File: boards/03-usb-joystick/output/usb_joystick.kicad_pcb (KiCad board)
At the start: 2 copper layers, 80 x 60 mm, 19 parts, among them J1 USB-C, J2 Joystick, SW1 Button, SW2 Button, SW3 Button, SW4 Button, U1 MCU, Y1 16MHz

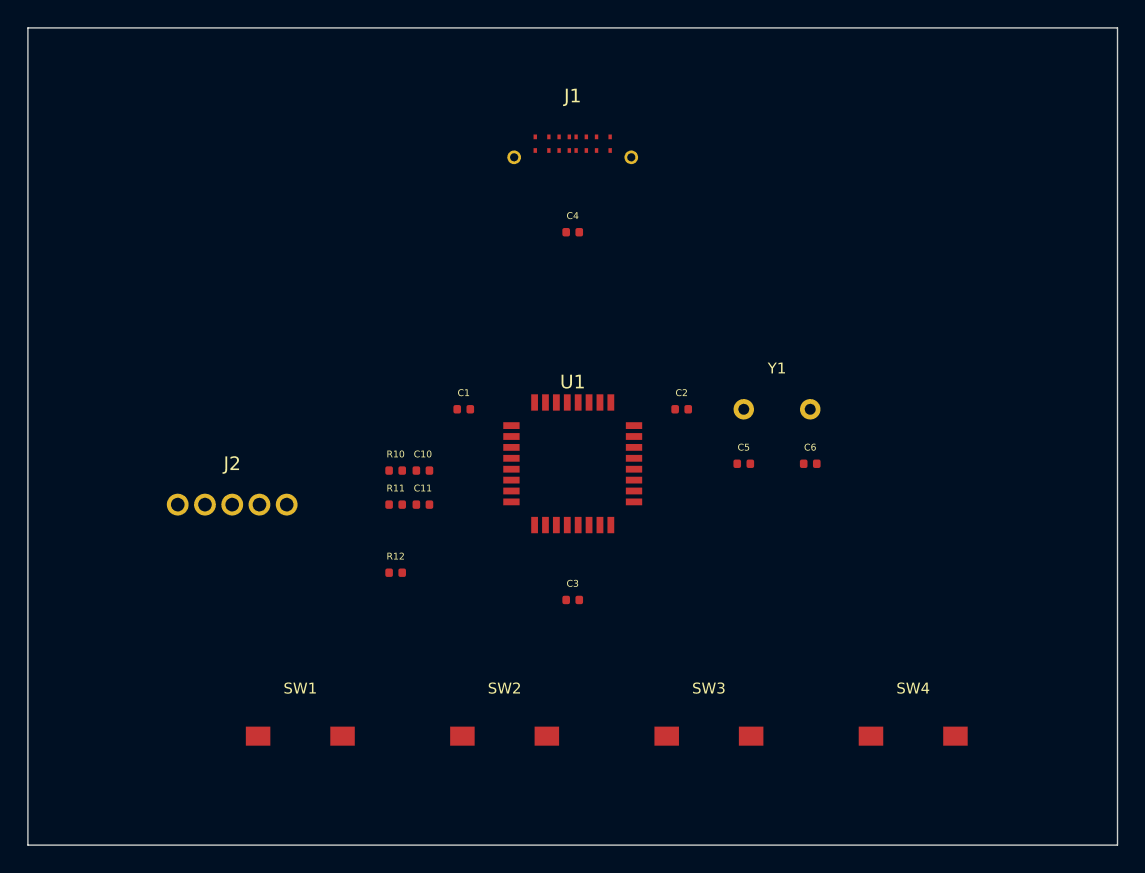
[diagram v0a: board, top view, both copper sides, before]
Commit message: feat(board-03): lock USB-C/SWD connectors and add B.Cu power pour (#2845)
Make boards/03-usb-joystick's source PCB a proper "anchor + ground
plane" starting point for the router:

- Mark J1 (USB-C, GCT_USB4105) `(attr smd locked)`. Without this,
  placement-feedback's centroid pull relocates the connector and
  starves VBUS/USB_CC1/USB_CC2 of routing corridors.
- Mark J2 (analog joystick header) `(attr through_hole locked)`. Same
  rationale for VCC/GND distribution to the joystick rail.
- Emit a B.Cu GND copper pour covering the board outline minus a
  0.5mm edge inset. Structurally required: board 03 has ~32 GND pads
  spread across decoupling caps, the joystick, J1's shield, and U1's
  unused pins. F.Cu signal traces alone cannot stitch them.

Sub-issue A of #2833 (decomposed). Subsequent sibling sub-issues
(#2837-#2840) handle grid auto-bump, single-ended ViaConflictManager
verification, --auto-fix engagement, and rollback contract.

Closes #2836
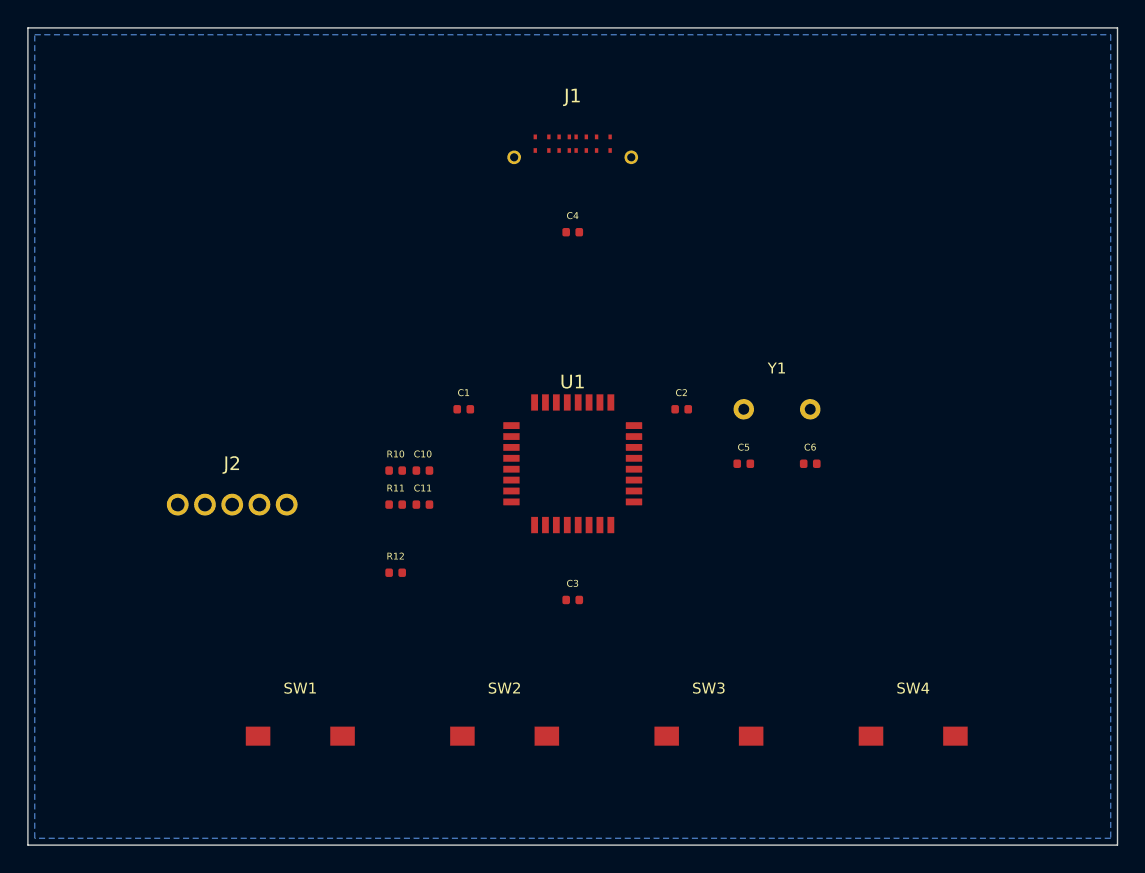
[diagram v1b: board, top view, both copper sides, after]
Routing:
- added copper zone on B.Cu, net GND
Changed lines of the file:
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@@
     (layer "F.Cu")
     (at 140.0 108.0)
+    (attr smd locked)
     (fp_text reference "J1" (at 0 -3) (layer "F.SilkS")
       (effects (font (size 1 1) (thickness 0.15)))
@@
     (layer "F.Cu")
     (at 115.0 135.0)
+    (attr through_hole locked)
     (fp_text reference "J2" (at 0 -3) (layer "F.SilkS")
       (effects (font (size 1 1) (thickness 0.15)))
@@
     (pad "2" smd roundrect (at 0.48 0) (size 0.56 0.62) (layers "F.Cu" "F.Paste" "F.Mask") (roundrect_rratio 0.25) (net 3 "GND"))
   )
+  (zone
+    (net 3)
+    (net_name "GND")
+    (layer "B.Cu")
+    (hatch edge 0.5)
+    (priority 1)
+    (connect_pads (clearance 0.3)
+    )
+    (min_thickness 0.25)
+    (filled_areas_thickness no)
+    (fill yes (thermal_gap 0.3) (thermal_bridge_width 0.4)
+    )
+    (polygon (pts (xy 100.5 100.5) (xy 179.5 100.5) (xy 179.5 159.5) (xy 100.5 159.5))
+    )
+  )
 )
